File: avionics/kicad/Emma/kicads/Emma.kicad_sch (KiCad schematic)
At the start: 78 parts, among them U1 ByA 100nF +3V3 U1-VDDA Bypass, U1 ByB 100nF +3V3 U1-VDD Bypass

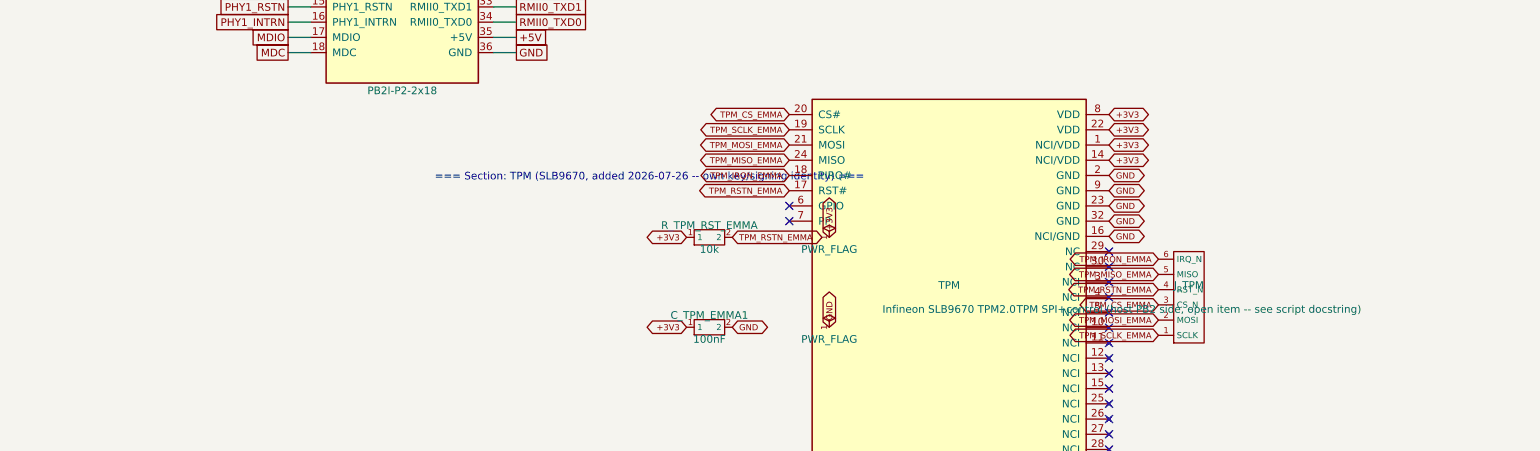
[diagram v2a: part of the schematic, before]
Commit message: CAN-PERIPH-GW-1: add stack orientation option; Emma: TPM binds to PB2 host via shared SPI1, not a dedicated header
CAN-PERIPH-GW-1:
- gen_can_periph_gw_pcb.py: new STACK_ORIENTATION setting ("END_TO_END",
  default, tiles along X / short-side-to-short-side, current behavior;
  "SIDE_BY_SIDE" tiles along Y / long-side-to-long-side for a wider,
  shorter board). Both pitches verified via sandboxed N_STACKS=4 dry runs
  (0 shorts/clearance/courtyard from placement).
- Synced ATTRIBUTION_POS to the position the user hand-corrected on the
  live board (the generator's first guess ran off the board corner).

Emma:
- TPM no longer gets a dedicated J_TPM header. Per design intent, the TPM
  provides the last/first cryptographic signature for radio messages Emma
  transmits and forwards, and binds to whichever PB2-I host Emma is
  stacked on (supporting self-sufficient, non-Serenity deployments) --
  so it taps the SPI1_CS_TPM/SPI1_CLK/SPI1_MOSI/SPI1_MISO +
  TPM_IRQN/TPM_RSTN nets already reserved on Emma's own P1/P2 trunk
  instead. Removed J_TPM/lib_symbol_j_tpm_emma() from the schematic and
  from inject_emma_tpm.py; retargeted the TPM/R_TPM_RST_EMMA footprints on
  the PCB to the corrected net names. ERC/DRC 0 hard after the rewire.

Co-Authored-By: Claude Sonnet 5 <noreply@anthropic.com>
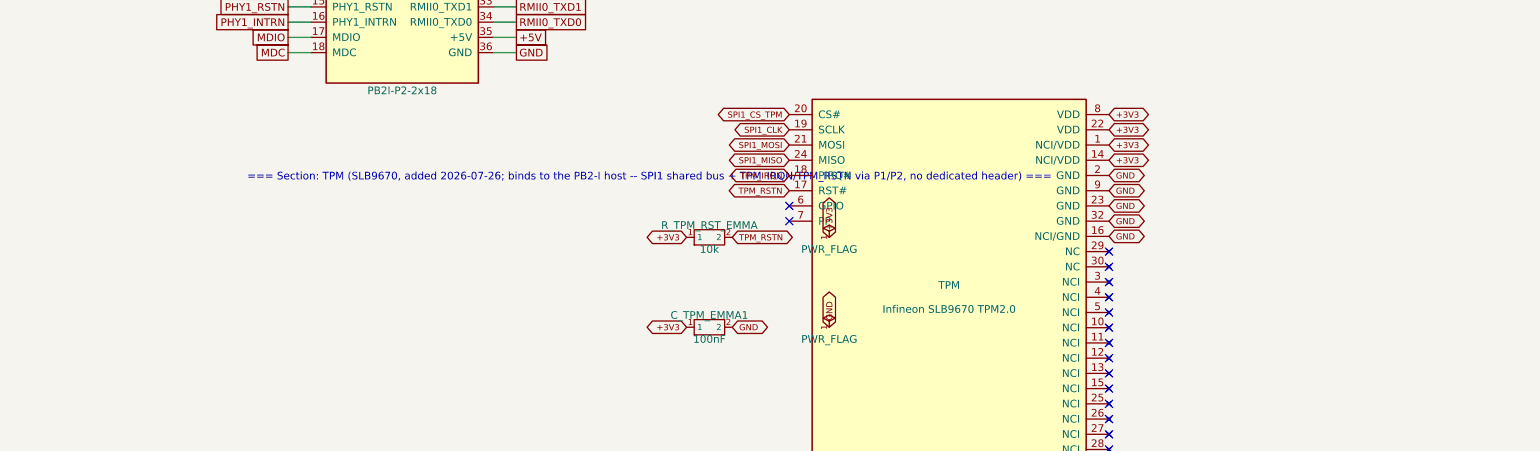
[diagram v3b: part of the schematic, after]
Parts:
- removed J_TPM: TPM SPI+control (host PB2 side, open item -- see 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, Connector_PinHeader_2.54mm:PinHeader_1x06_P2.54mm_Vertical, symbol J_TPM_EMMA
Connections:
- net TPM_CS_EMMA is gone; now on net SPI1_CS_TPM: TPM.20 (CS#)
- net TPM_IRQN_EMMA is gone; now on net TPM_IRQN: TPM.18 (PIRQ#)
- net TPM_MISO_EMMA is gone; now on net SPI1_MISO: TPM.24 (MISO)
- net TPM_MOSI_EMMA is gone; now on net SPI1_MOSI: TPM.21 (MOSI)
- net TPM_RSTN_EMMA is gone; now on net TPM_RSTN: R_TPM_RST_EMMA.2, TPM.17 (RST#)
- net TPM_SCLK_EMMA is gone; now on net SPI1_CLK: TPM.19 (SCLK)
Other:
- note added: "=== Section: TPM (SLB9670, added 2026-07-26; binds to the PB2-I host -- SPI1 shared bus + TPM_IRQN/TPM_RSTN via P1/P2, no dedicated header) ==="
- note removed: "=== Section: TPM (SLB9670, added 2026-07-26 -- own key/signing identity) ==="
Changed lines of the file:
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@@
   (wire (pts (xy 173.99 1059.18) (xy 177.80 1059.18)) (stroke (width 0) (type default)))
   (global_label "GND" (shape passive) (at 177.80 1059.18 0) (effects (font (size 1.27 1.27)) (justify left)))
-  (text "=== Section: TPM (SLB9670, added 2026-07-26 -- own key/signing identity) ===" (at 200.00 1080.00 0)
+  (text "=== Section: TPM (SLB9670, added 2026-07-26; binds to the PB2-I host -- SPI1 shared bus + TPM_IRQN/TPM_RSTN via P1/P2, no dedicated header) ===" (at 200.00 1080.00 0)
     (effects (font (size 1.27 1.27)))
 )
@@
       (effects (font (size 1.27 1.27)) (hide yes)))
   )
-  (global_label "TPM_CS_EMMA" (shape bidirectional) (at 223.33 1069.52 180)
+  (global_label "SPI1_CS_TPM" (shape bidirectional) (at 223.33 1069.52 180)
     (effects (font (size 1.016 1.016)))
     (property "Intersheet References" "${INTERSHEET_REFS}" (at 223.33 1069.52 0)
       (effects (font (size 1.016 1.016)) (hide yes))))
-  (global_label "TPM_SCLK_EMMA" (shape bidirectional) (at 223.33 1072.06 180)
+  (global_label "SPI1_CLK" (shape bidirectional) (at 223.33 1072.06 180)
     (effects (font (size 1.016 1.016)))
     (property "Intersheet References" "${INTERSHEET_REFS}" (at 223.33 1072.06 0)
       (effects (font (size 1.016 1.016)) (hide yes))))
-  (global_label "TPM_MOSI_EMMA" (shape bidirectional) (at 223.33 1074.60 180)
+  (global_label "SPI1_MOSI" (shape bidirectional) (at 223.33 1074.60 180)
     (effects (font (size 1.016 1.016)))
     (property "Intersheet References" "${INTERSHEET_REFS}" (at 223.33 1074.60 0)
       (effects (font (size 1.016 1.016)) (hide yes))))
-  (global_label "TPM_MISO_EMMA" (shape bidirectional) (at 223.33 1077.14 180)
+  (global_label "SPI1_MISO" (shape bidirectional) (at 223.33 1077.14 180)
     (effects (font (size 1.016 1.016)))
     (property "Intersheet References" "${INTERSHEET_REFS}" (at 223.33 1077.14 0)
       (effects (font (size 1.016 1.016)) (hide yes))))
-  (global_label "TPM_IRQN_EMMA" (shape bidirectional) (at 223.33 1079.68 180)
+  (global_label "TPM_IRQN" (shape bidirectional) (at 223.33 1079.68 180)
     (effects (font (size 1.016 1.016)))
     (property "Intersheet References" "${INTERSHEET_REFS}" (at 223.33 1079.68 0)
       (effects (font (size 1.016 1.016)) (hide yes))))
-  (global_label "TPM_RSTN_EMMA" (shape bidirectional) (at 223.33 1082.22 180)
+  (global_label "TPM_RSTN" (shape bidirectional) (at 223.33 1082.22 180)
     (effects (font (size 1.016 1.016)))
     (property "Intersheet References" "${INTERSHEET_REFS}" (at 223.33 1082.22 0)
@@
     (property "Intersheet References" "${INTERSHEET_REFS}" (at 206.19 1090.00 0)
       (effects (font (size 1.016 1.016)) (hide yes))))
-  (global_label "TPM_RSTN_EMMA" (shape bidirectional) (at 213.81 1090.00 0)
+  (global_label "TPM_RSTN" (shape bidirectional) (at 213.81 1090.00 0)
     (effects (font (size 1.016 1.016)))
     (property "Intersheet References" "${INTERSHEET_REFS}" (at 213.81 1090.00 0)
@@
     (property "Intersheet References" "${INTERSHEET_REFS}" (at 230.00 1105.00 0)
       (effects (font (size 1.016 1.016)) (hide yes))))
-  (symbol (lib_id "J_TPM_EMMA") (at 290.00 1100.00 0)
-    (unit 1) (exclude_from_sim no) (in_bom yes) (on_board yes) (dnp no)
-    (property "Reference" "J_TPM" (at 290.00 1098.00 0)
-      (effects (font (size 1.27 1.27))))
-    (property "Value" "TPM SPI+control (host PB2 side, open item -- see script docstring)" (at 290.00 1102.00 0)
-      (effects (font (size 1.27 1.27))))
-    (property "Footprint" "Connector_PinHeader_2.54mm:PinHeader_1x06_P2.54mm_Vertical" (at 0 0 0)
-      (effects (font (size 1.27 1.27)) (hide yes)))
-  )
-  (global_label "TPM_SCLK_EMMA" (shape bidirectional) (at 284.92 1106.35 180)
-    (effects (font (size 1.016 1.016)))
-    (property "Intersheet References" "${INTERSHEET_REFS}" (at 284.92 1106.35 0)
-      (effects (font (size 1.016 1.016)) (hide yes))))
-  (global_label "TPM_MOSI_EMMA" (shape bidirectional) (at 284.92 1103.81 180)
-    (effects (font (size 1.016 1.016)))
-    (property "Intersheet References" "${INTERSHEET_REFS}" (at 284.92 1103.81 0)
-      (effects (font (size 1.016 1.016)) (hide yes))))
-  (global_label "TPM_CS_EMMA" (shape bidirectional) (at 284.92 1101.27 180)
-    (effects (font (size 1.016 1.016)))
-    (property "Intersheet References" "${INTERSHEET_REFS}" (at 284.92 1101.27 0)
-      (effects (font (size 1.016 1.016)) (hide yes))))
-  (global_label "TPM_RSTN_EMMA" (shape bidirectional) (at 284.92 1098.73 180)
-    (effects (font (size 1.016 1.016)))
-    (property "Intersheet References" "${INTERSHEET_REFS}" (at 284.92 1098.73 0)
-      (effects (font (size 1.016 1.016)) (hide yes))))
-  (global_label "TPM_MISO_EMMA" (shape bidirectional) (at 284.92 1096.19 180)
-    (effects (font (size 1.016 1.016)))
-    (property "Intersheet References" "${INTERSHEET_REFS}" (at 284.92 1096.19 0)
-      (effects (font (size 1.016 1.016)) (hide yes))))
-  (global_label "TPM_IRQN_EMMA" (shape bidirectional) (at 284.92 1093.65 180)
-    (effects (font (size 1.016 1.016)))
-    (property "Intersheet References" "${INTERSHEET_REFS}" (at 284.92 1093.65 0)
-      (effects (font (size 1.016 1.016)) (hide yes))))
 )
